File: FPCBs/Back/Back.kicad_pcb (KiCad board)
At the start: 2 copper layers, 128 x 85.6 mm, 24 parts, among them J1 To PCB, J2 To Front, J3 Front, J4 EVF_SENSOR, J5 From LCD, SW1 MENU/SET, SW10 -+-, SW11 PLAY, SW12 WHEEL, SW13 S/C/M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

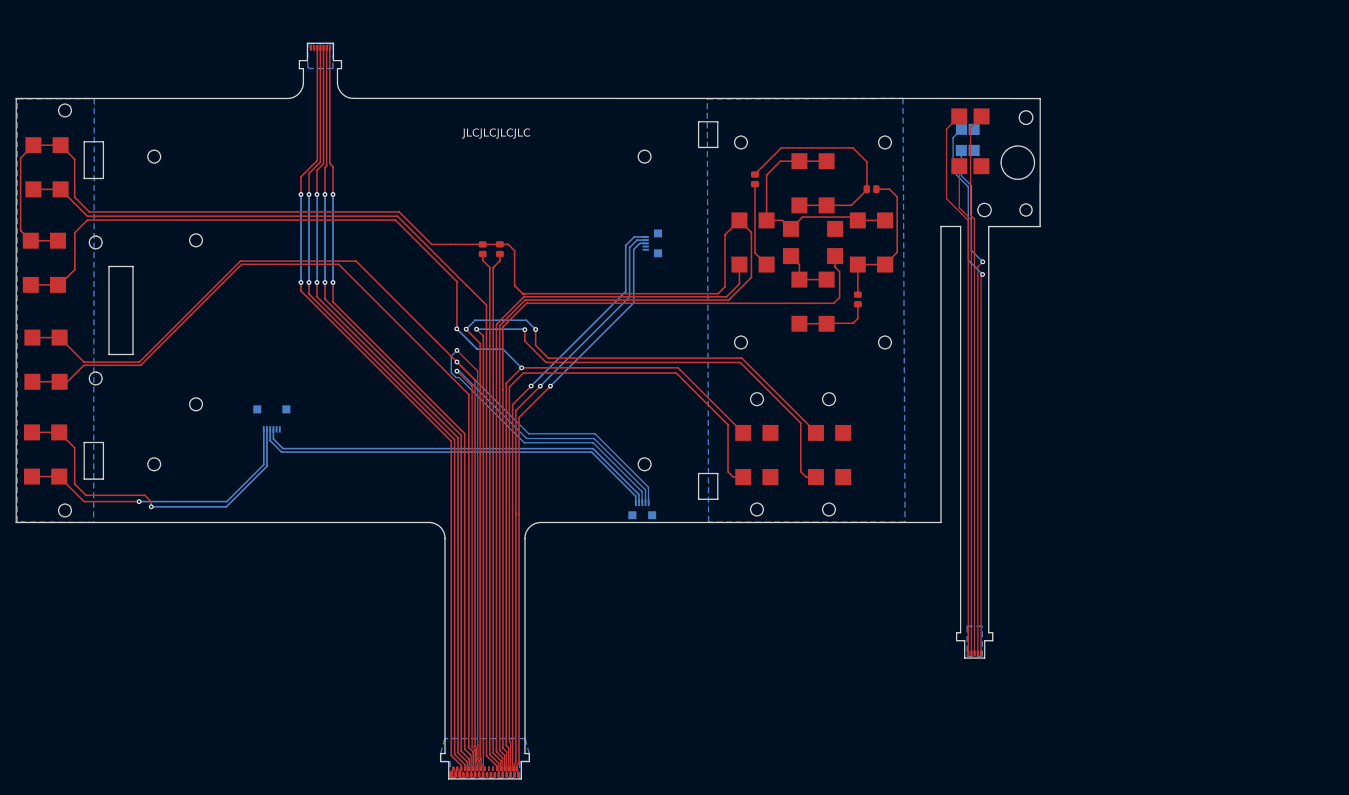
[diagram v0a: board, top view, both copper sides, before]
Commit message: Fix the buttons pins
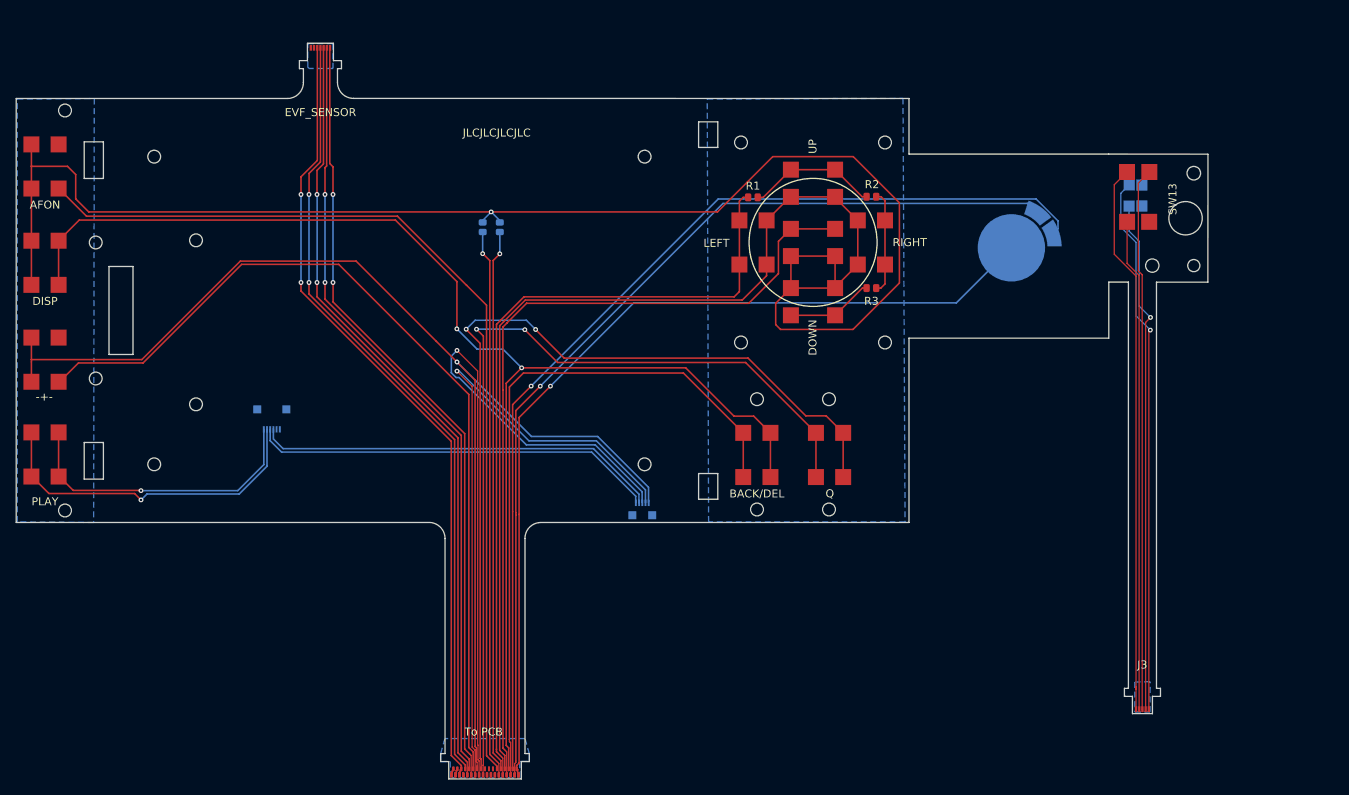
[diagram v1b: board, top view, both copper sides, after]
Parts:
- C1, C2: moved to B.Cu
- SW12: footprint Leica-G9ii:Connector-1Row-5Pins-0.40mm -> Leica-G9ii:back_dial
- moved SW12 44.9 mm to (183.8, 68.7)
- moved J3 22.1 mm to (200.2, 124.9)
- moved SW13 22.1 mm to (202.5, 62.3)
- moved SW14 22.1 mm to (200.8, 62.1)
- moved C1 2.75 mm to (117.7, 66.1)
- moved C2 2.75 mm to (119.8, 66.1)
- moved R1 2.27 mm to (151.5, 62.4), turned to 0 degrees
- moved R3 2.21 mm to (166.3, 73.7), turned to 0 degrees
- moved R2 0.94 mm to (166.3, 62.3)
- moved SW8 0.27 mm to (63.0, 58.5)
- moved SW10 0.12 mm to (63.0, 82.7)
- moved SW11 0.08 mm to (63.0, 94.5)
- moved SW9 0.08 mm to (63.0, 70.5)
- turned SW3 to -90 degrees
- turned SW4 to 180 degrees
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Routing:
- net Net-(J1-Pin_28): track 259.7 -> 313.6 mm, vias 0 -> 1
- net Net-(J1-Pin_32): track 74.2 -> 127.4 mm
- net Net-(J1-Pin_33): track 74.3 -> 121.9 mm
- net Net-(J1-Pin_34): track 73.7 -> 115.3 mm
- net Net-(SW5A-D): track 28.8 -> 16.6 mm
- net Net-(J1-Pin_16): track 107.0 -> 114.7 mm
- net Net-(SW2A-D): track 19.3 -> 13.0 mm
- net Net-(J1-Pin_30): track 160.8 -> 166.8 mm
- net Net-(J1-Pin_14): track 149.1 -> 153.3 mm
- net Net-(J1-Pin_12): track 114.4 -> 111.0 mm
- net Net-(J1-Pin_24): track 121.1 -> 118.0 mm
- net Net-(J1-Pin_25): track 65.9 -> 68.7 mm, vias 0 -> 1
- net Net-(J1-Pin_26): track 65.1 -> 67.9 mm, vias 0 -> 1
- net Net-(SW3A-D): track 9.36 -> 10.9 mm
- net Net-(J5-Pin_1): track 36.6 -> 37.6 mm
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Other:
- board size 128 x 85.6 mm -> 149 x 85.6 mm

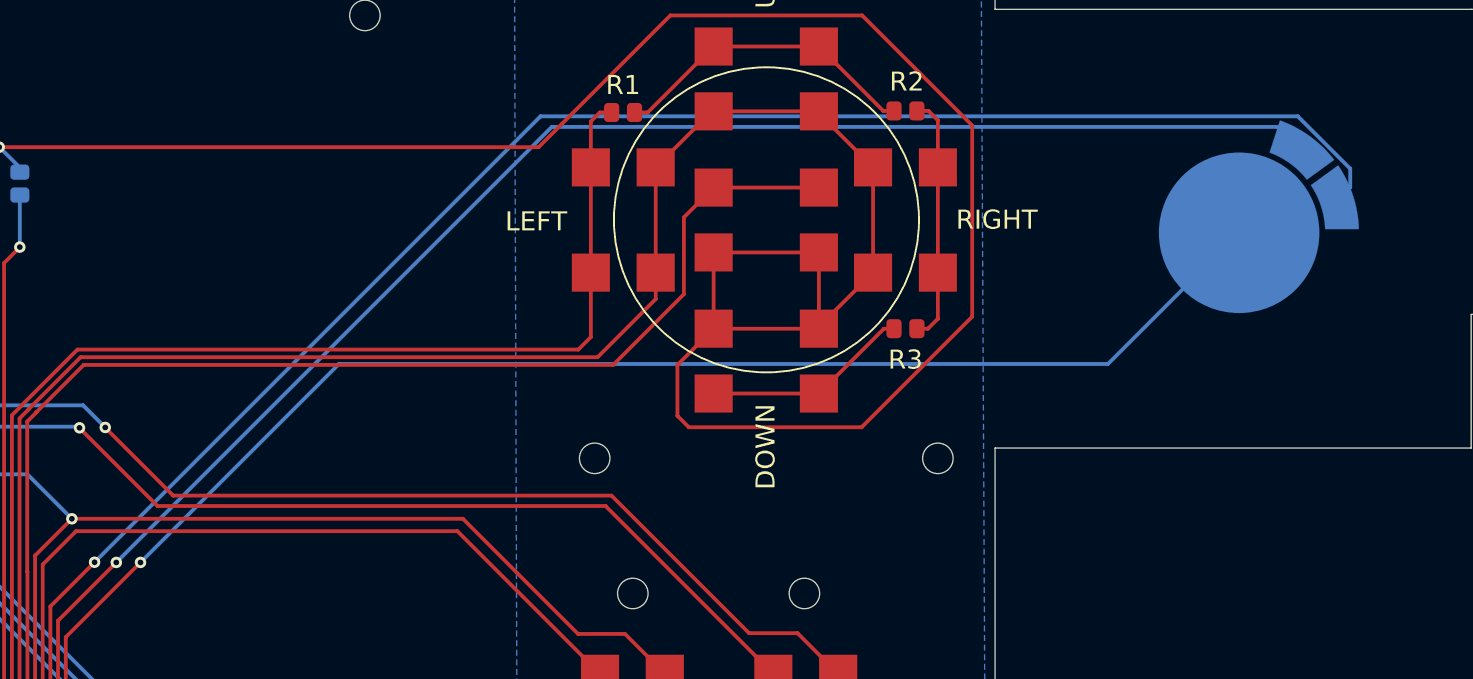
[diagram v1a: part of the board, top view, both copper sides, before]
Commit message: Fix back wheel footprint
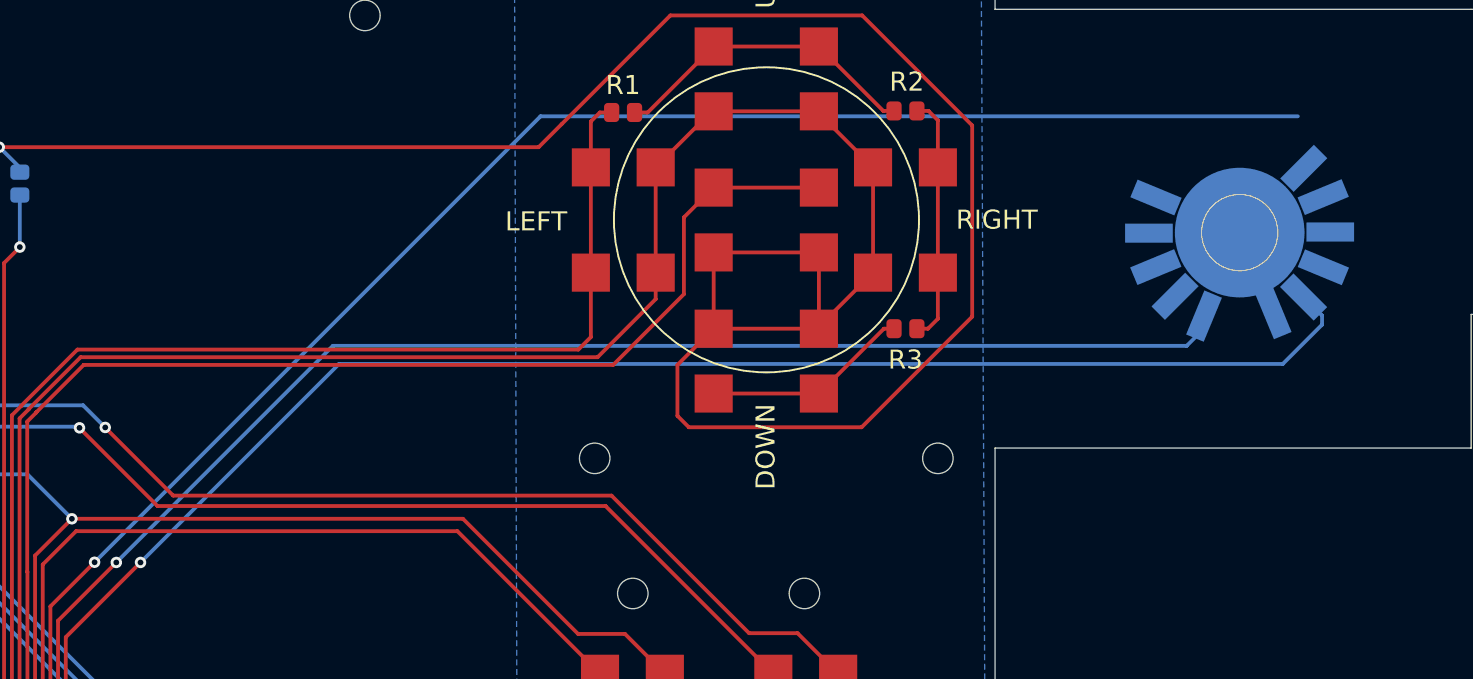
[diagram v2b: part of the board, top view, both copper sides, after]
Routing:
- net Net-(J1-Pin_33): track 121.9 -> 112.7 mm
- net Net-(J1-Pin_32): track 127.4 -> 121.6 mm
- net Net-(J1-Pin_34): track 115.3 -> 119.5 mm

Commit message: Fixes to Back board
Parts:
- moved SW12 16.2 mm to (200.0, 68.0), turned to 90 degrees
- moved J3 12.4 mm to (212.6, 125.0)
- moved SW13 12.4 mm to (214.9, 62.4)
- moved SW14 12.4 mm to (213.2, 62.2)
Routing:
- net Net-(J1-Pin_33): track 112.7 -> 130.6 mm
- net Net-(J1-Pin_34): track 119.5 -> 130.8 mm
- net Net-(J1-Pin_32): track 121.6 -> 130.1 mm
- net Net-(J5-Pin_1): track 37.6 -> 36.6 mm
- net Net-(J5-Pin_2): track 42.5 -> 41.5 mm
- added copper zone on F.Cu, net (none)
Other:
- board size 149 x 85.6 mm -> 161.4 x 85.6 mm

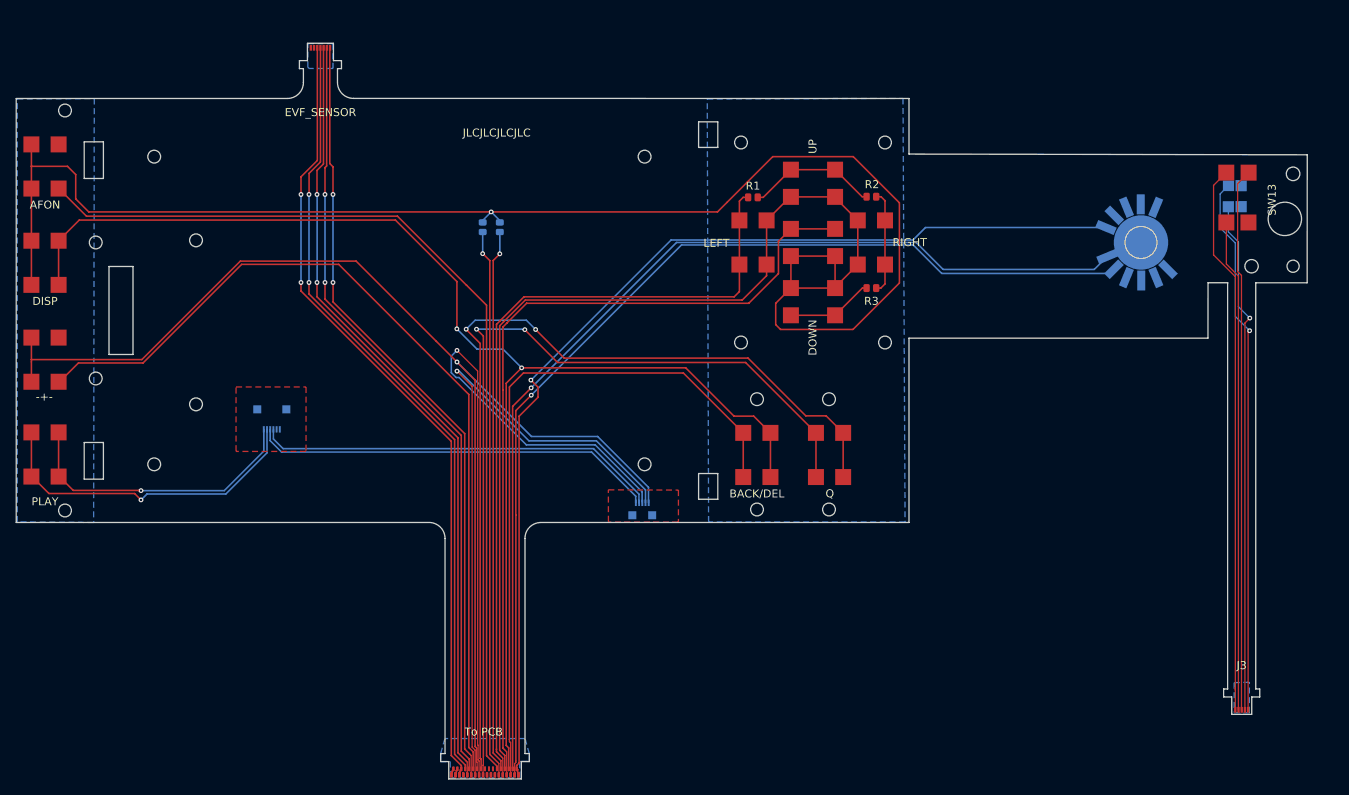
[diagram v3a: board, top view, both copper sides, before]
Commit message: Fixes to back pcb
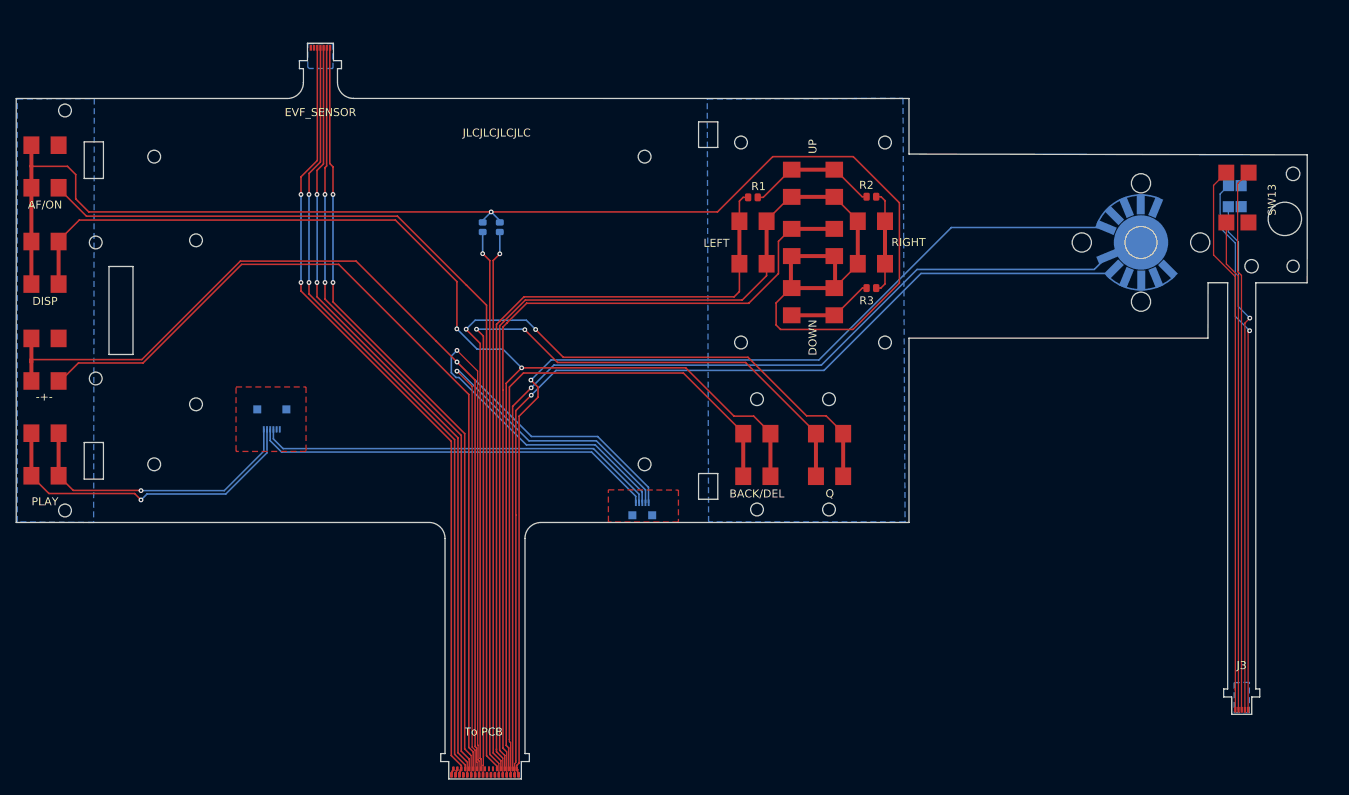
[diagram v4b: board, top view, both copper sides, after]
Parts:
- SW12: value WHEEL -> BACK WHEEL
- SW8: value AFON -> AF/ON
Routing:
- net Net-(J1-Pin_33): track 130.6 -> 127.7 mm
- net Net-(J1-Pin_32): track 130.1 -> 127.4 mm
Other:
- outline, holes or cut-outs redrawn

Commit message: Move evf sensor to left
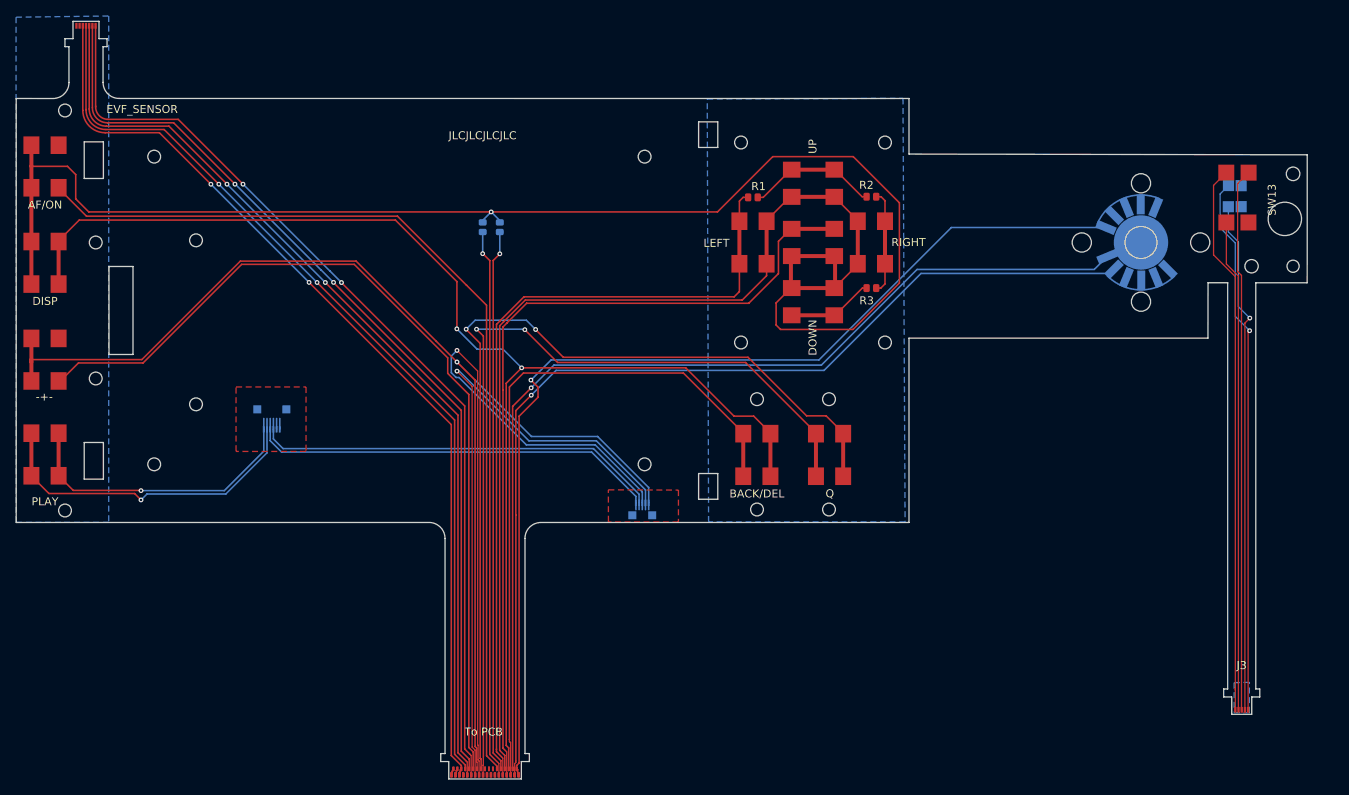
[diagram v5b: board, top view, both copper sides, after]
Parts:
- moved J4 29.4 mm to (68.1, 42.3)
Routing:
- net Net-(J1-Pin_11): track 98.4 -> 118.4 mm
- net Net-(J1-Pin_10): track 97.8 -> 117.5 mm
- net Net-(J1-Pin_9): track 99.2 -> 118.1 mm
- net Net-(J1-Pin_7): track 99.1 -> 117.1 mm
- net Net-(J1-Pin_5): track 100.3 -> 117.6 mm
- net Net-(J2-Pin_5): track 50.8 -> 53.0 mm
- net Net-(J2-Pin_4): track 50.8 -> 53.0 mm
- net unconnected-(J5-Pin_6-Pad6): track 0.00 -> 1.36 mm
- net unconnected-(J5-Pin_5-Pad5): track 0.00 -> 1.36 mm
- net Net-(J5-Pin_2): track 41.5 -> 42.8 mm
- net Net-(J5-Pin_1): track 36.6 -> 38.0 mm
- net Net-(J1-Pin_12): track 111.0 -> 112.1 mm
- net Net-(J1-Pin_14): track 153.3 -> 154.2 mm
- net Net-(J1-Pin_13): track 82.7 -> 83.6 mm
- net Net-(J1-Pin_15): track 88.7 -> 89.5 mm
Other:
- board size 161.4 x 85.6 mm -> 161.4 x 88.4 mm

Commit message: Fix back wheel
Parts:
- C1, C2, R1, R2, R3: footprint Leica-G9ii:R_2x1mm -> Leica-G9ii:R_0603
- SW12: value BACK WHEEL -> BACK_WHEEL
- moved SW13 3.20 mm to (218.1, 62.3)
- moved J3 3.20 mm to (215.8, 125.0)
- moved SW14 3.20 mm to (216.4, 62.2)
- moved R1 0.43 mm to (151.5, 62.8)
- moved R2 0.30 mm to (166.3, 62.6)
- moved R3 0.30 mm to (166.3, 73.4)
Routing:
- net Net-(J3-Pin_1): track 0.00 -> 81.2 mm
- net Net-(J3-Pin_2): track 130.8 -> 69.6 mm
- net Net-(J3-Pin_3): track 67.9 -> 61.7 mm
- net Net-(SW2A-D): track 13.0 -> 11.6 mm
- net Net-(J1-Pin_33): track 127.7 -> 128.9 mm
- net Net-(J1-Pin_27): track 101.3 -> 100.4 mm
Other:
- board size 161.4 x 88.4 mm -> 164.6 x 88.4 mm
